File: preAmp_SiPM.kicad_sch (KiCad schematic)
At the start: 15 parts, among them J3 Conn_01x02_Pin, J4 Conn_01x02_Pin, J5 Conn_01x02_Pin, J6 Conn_01x02_Pin, Q1 BFR92

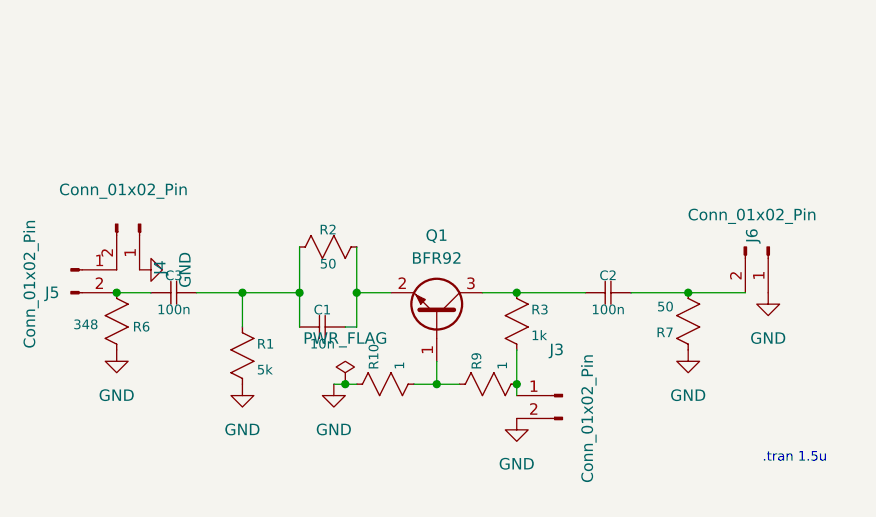
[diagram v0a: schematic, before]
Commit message: Adding a Capacitor and Design again the PCB
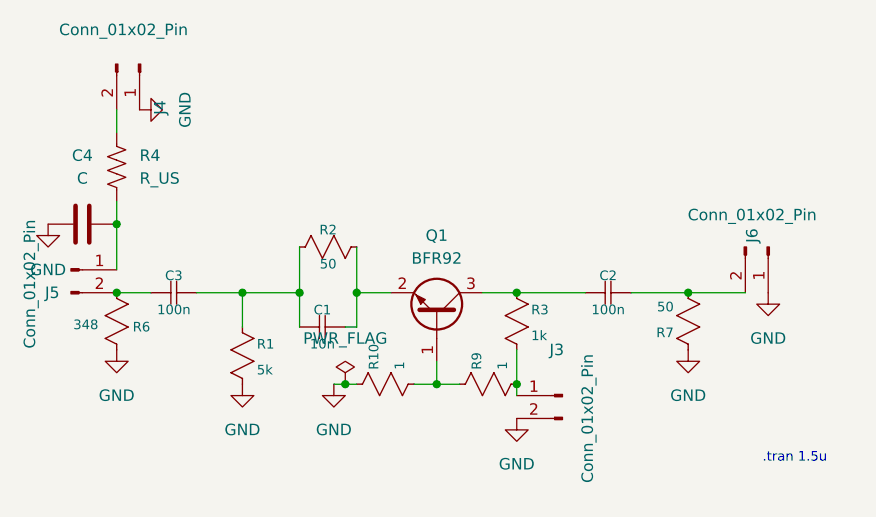
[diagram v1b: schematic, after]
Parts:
- added C4: C, Capacitor_SMD:C_0805_2012Metric_Pad1.18x1.45mm_HandSolder, symbol Device:C
- added R4: R_US, Resistor_SMD:R_0805_2012Metric_Pad1.20x1.40mm_HandSolder, symbol Device:R_US
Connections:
- net GND: now also C4.1
- net at J4.2 (Pin_2): now also R4.1; no longer J5.1 (Pin_1)
- new net: C4.2, J5.1 (Pin_1), R4.2
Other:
- moved on the sheet: J4
